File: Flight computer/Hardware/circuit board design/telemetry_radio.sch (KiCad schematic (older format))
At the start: 15 parts, among them J7 Conn_Coaxial, U2 0433BM41A0019E, U3 Si4463, X1 TM-32.000-AF3-33-S-Oscillator

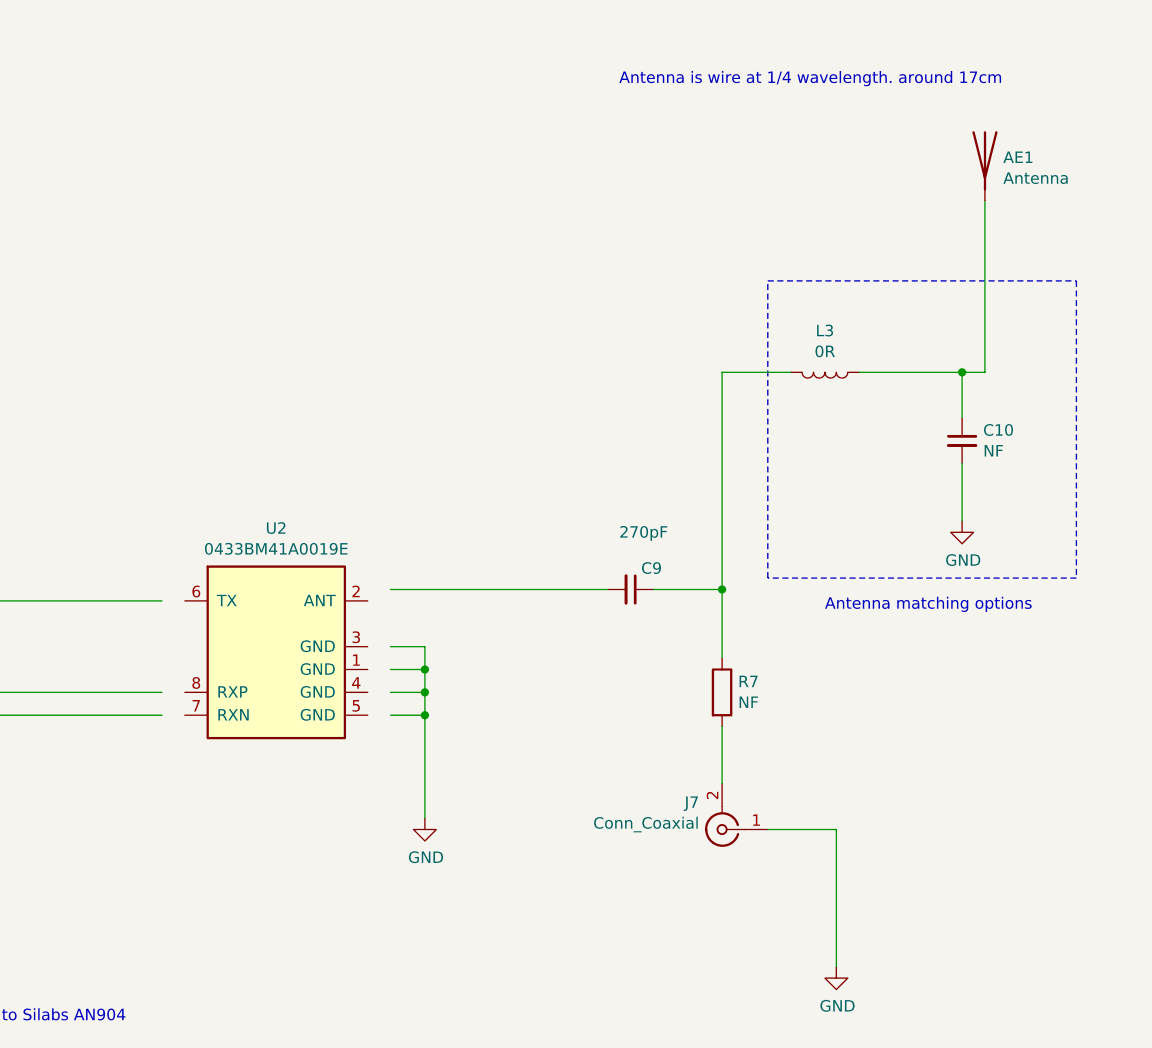
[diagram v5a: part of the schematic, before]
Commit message: standardised the symbol for the Johanson RF front end
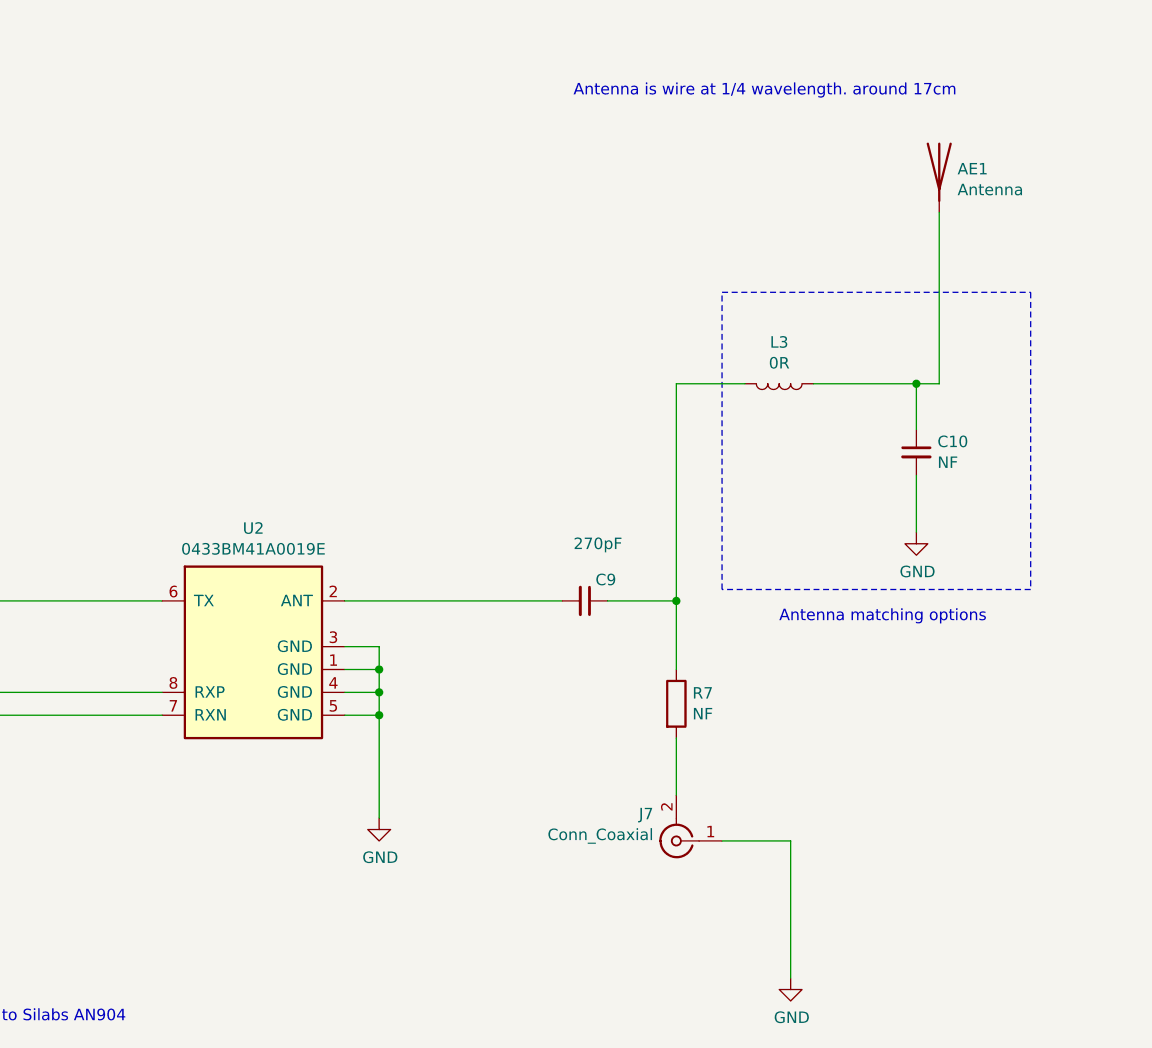
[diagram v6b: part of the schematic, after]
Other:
- moved on the sheet: AE1, C10, C9, J7, L3, R7, U2
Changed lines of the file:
@@
 L 0433BM41A0019E:0433BM41A0019E U2
 U 1 1 5D767292
-P 6450 4450
-F 0 "U2" H 6450 4967 50  0000 C CNN
-F 1 "0433BM41A0019E" H 6450 4876 50  0000 C CNN
-F 2 "Johanson_frontend:BALUN_0433BM41A0019E" H 5950 5100 50  0001 L BNN
-F 3 "https://www.johansontechnology.com/datasheets/0433BM41A0019/0433BM41A0019.pdf" H 5950 5100 50  0001 L BNN
-	1    6450 4450
+P 6350 4450
+F 0 "U2" H 6350 4967 50  0000 C CNN
+F 1 "0433BM41A0019E" H 6350 4876 50  0000 C CNN
+F 2 "Johanson_frontend:BALUN_0433BM41A0019E" H 5850 5100 50  0001 L BNN
+F 3 "https://www.johansontechnology.com/datasheets/0433BM41A0019/0433BM41A0019.pdf" H 5850 5100 50  0001 L BNN
+	1    6350 4450
 	1    0    0    -1
 $EndComp
@@
 	4200 4750 5950 4750
 Wire Wire Line
-	6950 4450 7100 4450
+	6750 4450 6900 4450
 Wire Wire Line
-	7100 4450 7100 4550
+	6900 4450 6900 4550
 Wire Wire Line
-	6950 4550 7100 4550
-Connection ~ 7100 4550
+	6750 4550 6900 4550
+Connection ~ 6900 4550
 Wire Wire Line
-	7100 4550 7100 4650
+	6900 4550 6900 4650
 Wire Wire Line
-	6950 4650 7100 4650
-Connection ~ 7100 4650
+	6750 4650 6900 4650
+Connection ~ 6900 4650
 Wire Wire Line
-	7100 4650 7100 4750
+	6900 4650 6900 4750
 Wire Wire Line
-	6950 4750 7100 4750
-Connection ~ 7100 4750
+	6750 4750 6900 4750
+Connection ~ 6900 4750
 Wire Wire Line
-	7100 4750 7100 5200
+	6900 4750 6900 5200
 Wire Notes Line
 	2950 3050 5000 3050
@@
 L power:GND #PWR016
 U 1 1 5D78B4ED
-P 7100 5200
-F 0 "#PWR016" H 7100 4950 50  0001 C CNN
-F 1 "GND" H 7105 5027 50  0000 C CNN
-F 2 "" H 7100 5200 50  0001 C CNN
-F 3 "" H 7100 5200 50  0001 C CNN
-	1    7100 5200
+P 6900 5200
+F 0 "#PWR016" H 6900 4950 50  0001 C CNN
+F 1 "GND" H 6905 5027 50  0000 C CNN
+F 2 "" H 6900 5200 50  0001 C CNN
+F 3 "" H 6900 5200 50  0001 C CNN
+	1    6900 5200
 	1    0    0    -1
 $EndComp
 Wire Wire Line
-	6950 4200 7900 4200
+	6750 4250 7700 4250
 $Comp
 L Device:C_Small C9
 U 1 1 5D796ABE
-P 8000 4200
-F 0 "C9" V 8092 4246 50  0000 L CNN
-F 1 "270pF" V 8250 4150 50  0000 L CNN
-F 2 "Capacitor_SMD:C_0402_1005Metric" H 8000 4200 50  0001 C CNN
-F 3 "~" H 8000 4200 50  0001 C CNN
-	1    8000 4200
+P 7800 4250
+F 0 "C9" V 7892 4296 50  0000 L CNN
+F 1 "270pF" V 8050 4200 50  0000 L CNN
+F 2 "Capacitor_SMD:C_0402_1005Metric" H 7800 4250 50  0001 C CNN
+F 3 "~" H 7800 4250 50  0001 C CNN
+	1    7800 4250
 	0    1    -1   0
 $EndComp
@@
 NoConn ~ 4200 5250
 NoConn ~ 4200 5150
-Text Notes 7950 2000 0    50   ~ 0
+Text Notes 7750 2050 0    50   ~ 0
 Antenna is wire at 1/4 wavelength. around 17cm
 Text Notes 4550 6100 0    50   ~ 0
 Arranged according to Silabs AN904
 Wire Notes Line
-	9950 2850 9950 4150
+	9750 2900 9750 4200
 Wire Notes Line
-	8600 2850 9950 2850
+	8400 2900 9750 2900
 Wire Notes Line
-	8600 4150 8600 2850
+	8400 4200 8400 2900
 Wire Notes Line
-	9950 4150 8600 4150
+	9750 4200 8400 4200
 $Comp
 L Device:L L3
 U 1 1 5D7F0545
-P 8850 3250
-F 0 "L3" V 8669 3250 50  0000 C CNN
-F 1 "0R" V 8760 3250 50  0000 C CNN
-F 2 "Inductor_SMD:L_0402_1005Metric" H 8850 3250 50  0001 C CNN
-F 3 "~" H 8850 3250 50  0001 C CNN
-	1    8850 3250
+P 8650 3300
+F 0 "L3" V 8469 3300 50  0000 C CNN
+F 1 "0R" V 8560 3300 50  0000 C CNN
+F 2 "Inductor_SMD:L_0402_1005Metric" H 8650 3300 50  0001 C CNN
+F 3 "~" H 8650 3300 50  0001 C CNN
+	1    8650 3300
 	0    1    1    0
 $EndComp
 Wire Wire Line
-	8400 3250 8700 3250
-Text Notes 8850 4300 0    50   ~ 0
+	8200 3300 8500 3300
+Text Notes 8650 4350 0    50   ~ 0
 Antenna matching options\n
 Wire Wire Line
-	9450 3250 9550 3250
-Connection ~ 9450 3250
+	9250 3300 9350 3300
+Connection ~ 9250 3300
 Wire Wire Line
-	9450 3250 9450 3450
+	9250 3300 9250 3500
 $Comp
 L power:GND #PWR07
 U 1 1 5D7EC7E0
-P 9450 3900
-F 0 "#PWR07" H 9450 3650 50  0001 C CNN
-F 1 "GND" H 9455 3727 50  0000 C CNN
-F 2 "" H 9450 3900 50  0001 C CNN
-F 3 "" H 9450 3900 50  0001 C CNN
-	1    9450 3900
+P 9250 3950
+F 0 "#PWR07" H 9250 3700 50  0001 C CNN
+F 1 "GND" H 9255 3777 50  0000 C CNN
+F 2 "" H 9250 3950 50  0001 C CNN
+F 3 "" H 9250 3950 50  0001 C CNN
+	1    9250 3950
 	1    0    0    -1
 $EndComp
@@
 L Device:C_Small C10
 U 1 1 5D7EC7D6
-P 9450 3550
-F 0 "C10" H 9358 3596 50  0000 R CNN
-F 1 "NF" H 9358 3505 50  0000 R CNN
-F 2 "Capacitor_SMD:C_0603_1608Metric" H 9450 3550 50  0001 C CNN
-F 3 "~" H 9450 3550 50  0001 C CNN
-	1    9450 3550
+P 9250 3600
+F 0 "C10" H 9158 3646 50  0000 R CNN
+F 1 "NF" H 9158 3555 50  0000 R CNN
+F 2 "Capacitor_SMD:C_0603_1608Metric" H 9250 3600 50  0001 C CNN
+F 3 "~" H 9250 3600 50  0001 C CNN
+	1    9250 3600
 	-1   0    0    -1
 $EndComp
 Wire Wire Line
-	9450 3650 9450 3900
+	9250 3700 9250 3950
 Wire Wire Line
-	8400 3250 8400 4200
+	8200 3300 8200 4250
 Wire Wire Line
-	9000 3250 9450 3250
+	8800 3300 9250 3300
 Wire Wire Line
-	8400 4800 8400 5050
+	8200 4850 8200 5100
 $Comp
 L Device:R R7
 U 1 1 5D7AB0E5
-P 8400 4650
-F 0 "R7" H 8470 4696 50  0000 L CNN
-F 1 "NF" H 8470 4605 50  0000 L CNN
-F 2 "Resistor_SMD:R_0402_1005Metric" V 8330 4650 50  0001 C CNN
-F 3 "~" H 8400 4650 50  0001 C CNN
-	1    8400 4650
+P 8200 4700
+F 0 "R7" H 8270 4746 50  0000 L CNN
+F 1 "NF" H 8270 4655 50  0000 L CNN
+F 2 "Resistor_SMD:R_0402_1005Metric" V 8130 4700 50  0001 C CNN
+F 3 "~" H 8200 4700 50  0001 C CNN
+	1    8200 4700
 	1    0    0    -1
 $EndComp
@@
 L power:GND #PWR028
 U 1 1 5D7A6387
-P 8900 5850
-F 0 "#PWR028" H 8900 5600 50  0001 C CNN
-F 1 "GND" H 8905 5677 50  0000 C CNN
-F 2 "" H 8900 5850 50  0001 C CNN
-F 3 "" H 8900 5850 50  0001 C CNN
-	1    8900 5850
+P 8700 5900
+F 0 "#PWR028" H 8700 5650 50  0001 C CNN
+F 1 "GND" H 8705 5727 50  0000 C CNN
+F 2 "" H 8700 5900 50  0001 C CNN
+F 3 "" H 8700 5900 50  0001 C CNN
+	1    8700 5900
 	1    0    0    -1
 $EndComp
 Wire Wire Line
-	8900 5250 8900 5850
+	8700 5300 8700 5900
 Wire Wire Line
-	8600 5250 8900 5250
+	8400 5300 8700 5300
 $Comp
 L Connector:Conn_Coaxial J7
 U 1 1 5D7A2CE8
-P 8400 5250
-F 0 "J7" H 8500 5132 50  0000 L CNN
-F 1 "Conn_Coaxial" H 8500 5223 50  0000 L CNN
-F 2 "Connector_Coaxial:U.FL_Hirose_U.FL-R-SMT-1_Vertical" H 8400 5250 50  0001 C CNN
-F 3 " ~" H 8400 5250 50  0001 C CNN
-	1    8400 5250
+P 8200 5300
+F 0 "J7" H 8300 5182 50  0000 L CNN
+F 1 "Conn_Coaxial" H 8300 5273 50  0000 L CNN
+F 2 "Connector_Coaxial:U.FL_Hirose_U.FL-R-SMT-1_Vertical" H 8200 5300 50  0001 C CNN
+F 3 " ~" H 8200 5300 50  0001 C CNN
+	1    8200 5300
 	-1   0    0    1
 $EndComp
-Connection ~ 8400 4200
+Connection ~ 8200 4250
 Wire Wire Line
-	8400 4200 8400 4500
+	8200 4250 8200 4550
 Wire Wire Line
-	8100 4200 8400 4200
+	7900 4250 8200 4250
 Wire Wire Line
-	9550 2500 9550 3250
+	9350 2550 9350 3300
 $Comp
 L Device:Antenna AE1
 U 1 1 5D79EB91
-P 9550 2300
-F 0 "AE1" H 9630 2289 50  0000 L CNN
-F 1 "Antenna" H 9630 2198 50  0000 L CNN
-F 2 "Connector_PinHeader_1.00mm:PinHeader_1x03_P1.00mm_Vertical" H 9550 2300 50  0001 C CNN
-F 3 "~" H 9550 2300 50  0001 C CNN
-	1    9550 2300
+P 9350 2350
+F 0 "AE1" H 9430 2339 50  0000 L CNN
+F 1 "Antenna" H 9430 2248 50  0000 L CNN
+F 2 "Connector_PinHeader_1.00mm:PinHeader_1x03_P1.00mm_Vertical" H 9350 2350 50  0001 C CNN
+F 3 "~" H 9350 2350 50  0001 C CNN
+	1    9350 2350
 	1    0    0    -1
 $EndComp

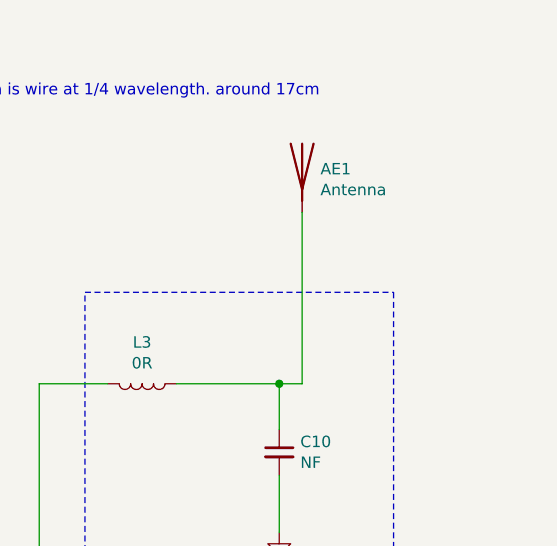
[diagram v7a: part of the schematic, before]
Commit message: swapped out the 434 wire antenna for a Yageo434 chip antenna for smaller form factor
I put in the 3D model for the te connectivity terminal blocks
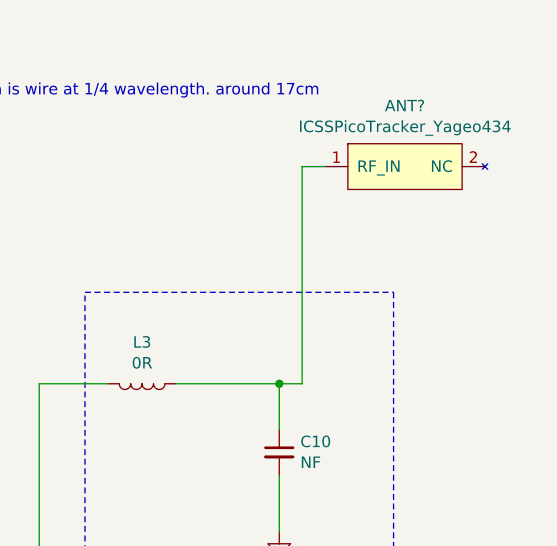
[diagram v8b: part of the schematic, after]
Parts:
- removed AE1: Antenna, Connector_PinHeader_1.00mm:PinHeader_1x03_P1.00mm_Vertical, symbol Device:Antenna
- added ANT?: ICSSPicoTracker_Yageo434, symbol flight-computer:ICSSPicoTracker_Yageo434
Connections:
- net at C10.1, L3.1: now also ANT?.1 (RF_IN)
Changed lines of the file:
@@
 Wire Wire Line
 	7900 4250 8200 4250
-Wire Wire Line
-	9350 2550 9350 3300
-$Comp
-L Device:Antenna AE1
-U 1 1 5D79EB91
-P 9350 2350
-F 0 "AE1" H 9430 2339 50  0000 L CNN
-F 1 "Antenna" H 9430 2248 50  0000 L CNN
-F 2 "Connector_PinHeader_1.00mm:PinHeader_1x03_P1.00mm_Vertical" H 9350 2350 50  0001 C CNN
-F 3 "~" H 9350 2350 50  0001 C CNN
-	1    9350 2350
-	1    0    0    -1
-$EndComp
 $Comp
 L Connector:Conn_Coaxial J7
@@
 	1    0    0    -1
 $EndComp
+$Comp
+L flight-computer:ICSSPicoTracker_Yageo434 ANT?
+U 1 1 5DB119FE
+P 9850 2350
+F 0 "ANT?" H 9800 2615 50  0000 C CNN
+F 1 "ICSSPicoTracker_Yageo434" H 9800 2524 50  0000 C CNN
+F 2 "" H 9850 2350 50  0001 C CNN
+F 3 "" H 9850 2350 50  0001 C CNN
+	1    9850 2350
+	1    0    0    -1
+$EndComp
+Wire Wire Line
+	9350 2350 9450 2350
+Wire Wire Line
+	9350 2350 9350 3300
 $EndSCHEMATC
